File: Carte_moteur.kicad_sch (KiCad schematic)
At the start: 9 parts, among them J101 Conn_01x02, J102 Conn_01x02, J103 Conn_01x02_Socket, U403 LD1117S33TR_SOT223

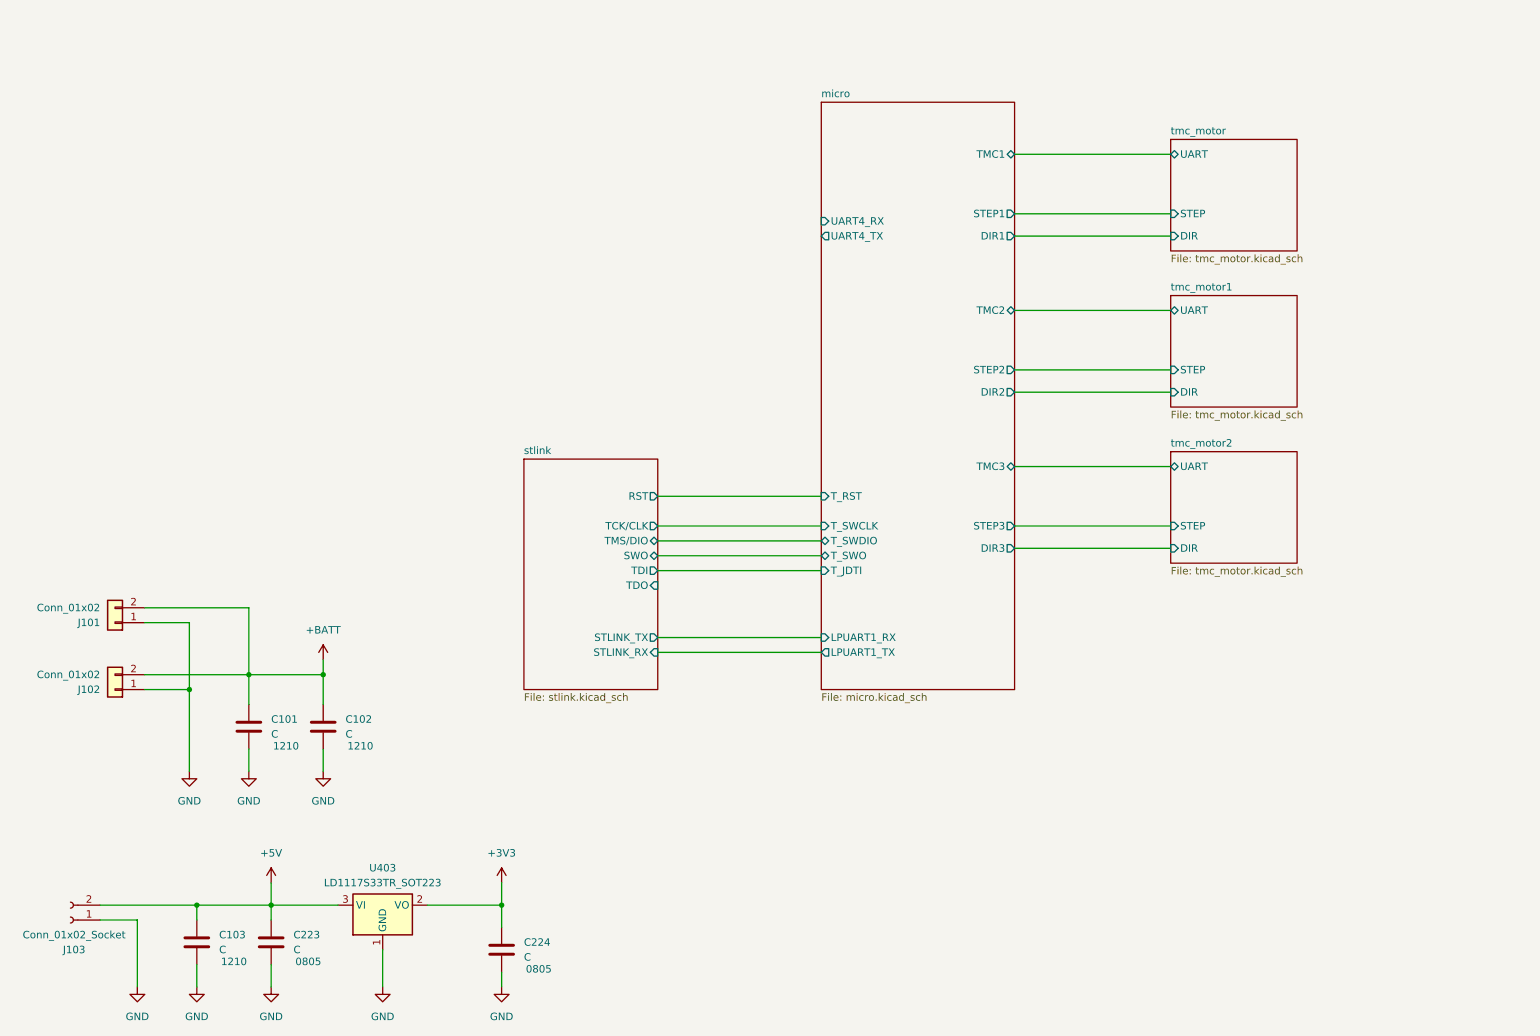
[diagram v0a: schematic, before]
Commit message: Added SPI
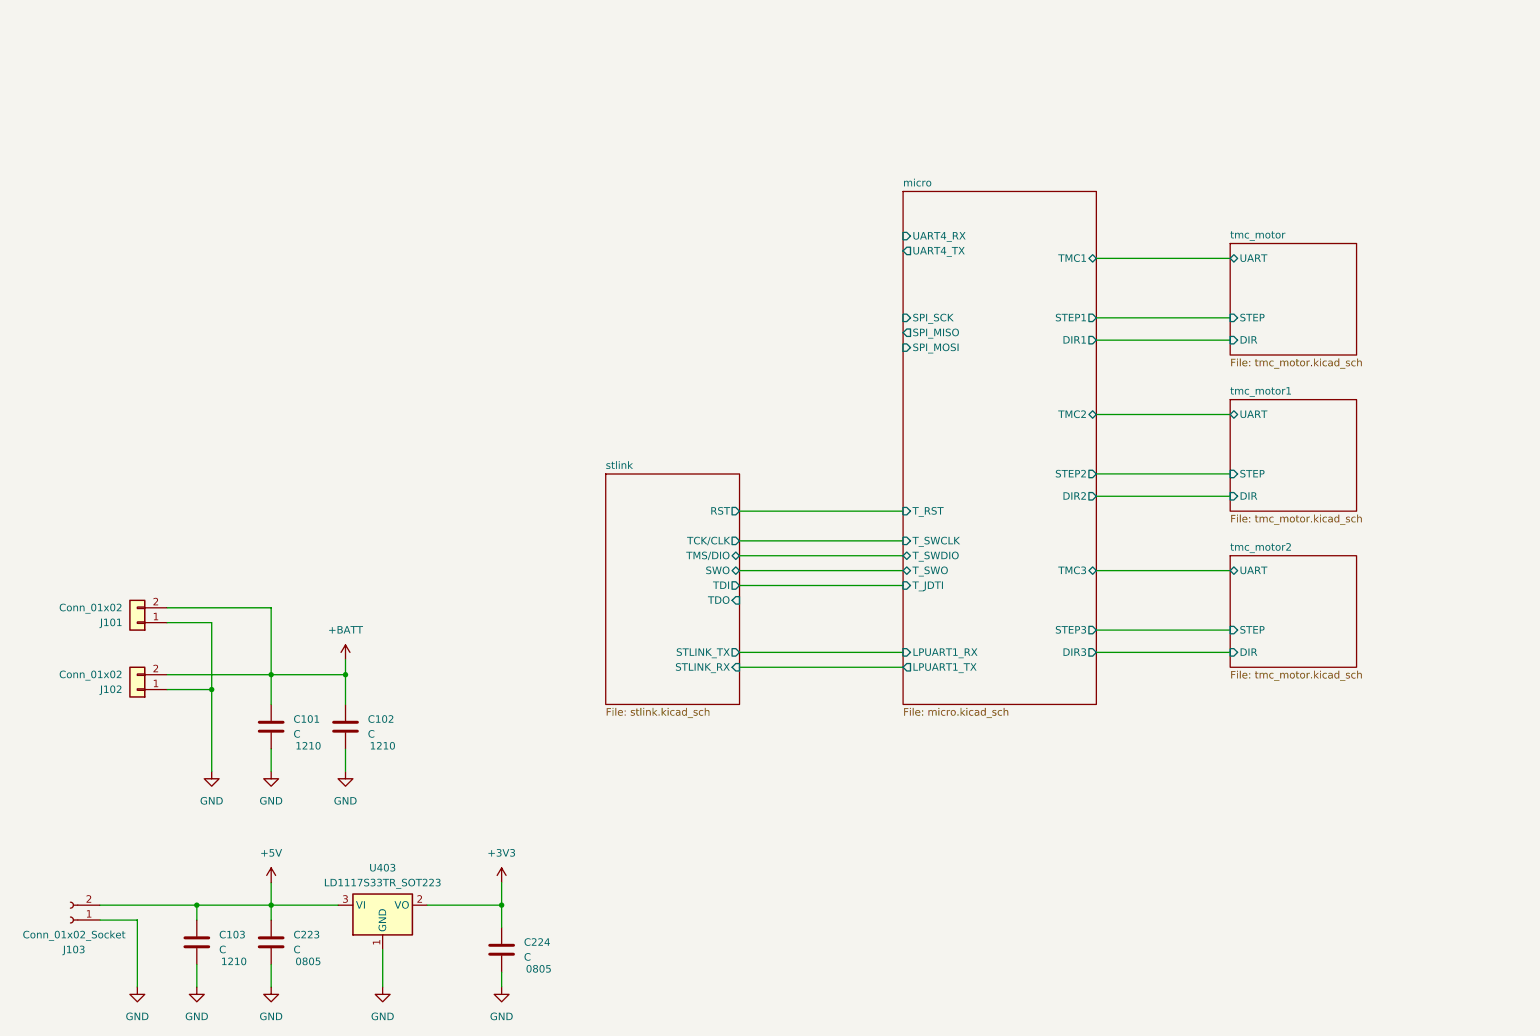
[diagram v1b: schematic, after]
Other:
- sheet micro ports: added SPI_MISO, SPI_MOSI, SPI_SCK; removed none
- moved on the sheet: C101, C102, J101, J102

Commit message: starting layout
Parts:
- J102: renamed from J101; footprint (none) -> Connector_Molex:Molex_KK-396_A-41791-0002_1x02_P3.96mm_Vertical
- J103: renamed from J102; footprint (none) -> Connector_Molex:Molex_KK-396_A-41791-0002_1x02_P3.96mm_Vertical
- renumbered C103 to C101, C101 to C102, C223 to C103, C102 to C104, C224 to C105, J103 to J101, U403 to U101
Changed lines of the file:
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@@
 		(dnp no)
 		(fields_autoplaced yes)
-		(property "Reference" "#PWR0284"
+		(property "Reference" "#PWR0107"
 			(at 71.12 133.35 0)
 			(effects
@@
 			(project "Carte_moteur"
 				(path "/5d858058-eb89-4613-a7ba-0652b9f0936c"
-					(reference "#PWR0284")
+					(reference "#PWR0107")
 					(unit 1)
 				)
@@
 		(on_board yes)
 		(dnp no)
-		(property "Reference" "C223"
+		(property "Reference" "C103"
 			(at 62.23 176.5299 0)
 			(effects
@@
 			(project "Carte_moteur"
 				(path "/5d858058-eb89-4613-a7ba-0652b9f0936c"
-					(reference "C223")
+					(reference "C103")
 					(unit 1)
 				)
@@
 		(dnp no)
 		(fields_autoplaced yes)
-		(property "Reference" "#PWR0291"
+		(property "Reference" "#PWR0110"
 			(at 97.79 171.45 0)
 			(effects
@@
 			(project "Carte_moteur"
 				(path "/5d858058-eb89-4613-a7ba-0652b9f0936c"
-					(reference "#PWR0291")
+					(reference "#PWR0110")
 					(unit 1)
 				)
@@
 		(on_board yes)
 		(dnp no)
-		(property "Reference" "C103"
+		(property "Reference" "C101"
 			(at 49.53 176.5299 0)
 			(effects
@@
 			(project "Carte_moteur"
 				(path "/5d858058-eb89-4613-a7ba-0652b9f0936c"
-					(reference "C103")
+					(reference "C101")
 					(unit 1)
 				)
@@
 		(dnp no)
 		(fields_autoplaced yes)
-		(property "Reference" "#PWR0293"
+		(property "Reference" "#PWR0101"
 			(at 35.56 191.77 0)
 			(effects
@@
 			(project "Carte_moteur"
 				(path "/5d858058-eb89-4613-a7ba-0652b9f0936c"
-					(reference "#PWR0293")
+					(reference "#PWR0101")
 					(unit 1)
 				)
@@
 		(on_board yes)
 		(dnp no)
-		(property "Reference" "C101"
+		(property "Reference" "C102"
 			(at 62.23 139.6999 0)
 			(effects
@@
 			(project "Carte_moteur"
 				(path "/5d858058-eb89-4613-a7ba-0652b9f0936c"
-					(reference "C101")
+					(reference "C102")
 					(unit 1)
 				)
@@
 		(on_board yes)
 		(dnp no)
-		(property "Reference" "J101"
+		(property "Reference" "J102"
 			(at 33.02 123.1901 0)
 			(effects
@@
 			)
 		)
-		(property "Footprint" ""
+		(property "Footprint" "Connector_Molex:Molex_KK-396_A-41791-0002_1x02_P3.96mm_Vertical"
 			(at 35.56 123.19 0)
 			(effects
@@
 			(project ""
 				(path "/5d858058-eb89-4613-a7ba-0652b9f0936c"
-					(reference "J101")
+					(reference "J102")
 					(unit 1)
 				)
@@
 		(dnp no)
 		(fields_autoplaced yes)
-		(property "Reference" "#PWR0289"
+		(property "Reference" "#PWR0109"
 			(at 77.47 191.77 0)
 			(effects
@@
 			(project "Carte_moteur"
 				(path "/5d858058-eb89-4613-a7ba-0652b9f0936c"
-					(reference "#PWR0289")
+					(reference "#PWR0109")
 					(unit 1)
 				)
@@
 		(on_board yes)
 		(dnp no)
-		(property "Reference" "#PWR0286"
+		(property "Reference" "#PWR0108"
 			(at 71.12 154.94 0)
 			(effects
@@
 			(project "Carte_moteur"
 				(path "/5d858058-eb89-4613-a7ba-0652b9f0936c"
-					(reference "#PWR0286")
+					(reference "#PWR0108")
 					(unit 1)
 				)
@@
 		(dnp no)
 		(fields_autoplaced yes)
-		(property "Reference" "#PWR0416"
+		(property "Reference" "#PWR0105"
 			(at 58.42 171.45 0)
 			(effects
@@
 			(project "Carte_moteur"
 				(path "/5d858058-eb89-4613-a7ba-0652b9f0936c"
-					(reference "#PWR0416")
+					(reference "#PWR0105")
 					(unit 1)
 				)
@@
 		(on_board yes)
 		(dnp no)
-		(property "Reference" "C102"
+		(property "Reference" "C104"
 			(at 74.93 139.6999 0)
 			(effects
@@
 			(project "Carte_moteur"
 				(path "/5d858058-eb89-4613-a7ba-0652b9f0936c"
-					(reference "C102")
+					(reference "C104")
 					(unit 1)
 				)
@@
 		(on_board yes)
 		(dnp no)
-		(property "Reference" "#PWR0287"
+		(property "Reference" "#PWR0103"
 			(at 48.26 154.94 0)
 			(effects
@@
 			(project "Carte_moteur"
 				(path "/5d858058-eb89-4613-a7ba-0652b9f0936c"
-					(reference "#PWR0287")
+					(reference "#PWR0103")
 					(unit 1)
 				)
@@
 		(on_board yes)
 		(dnp no)
-		(property "Reference" "#PWR0285"
+		(property "Reference" "#PWR0104"
 			(at 58.42 154.94 0)
 			(effects
@@
 			(project "Carte_moteur"
 				(path "/5d858058-eb89-4613-a7ba-0652b9f0936c"
-					(reference "#PWR0285")
+					(reference "#PWR0104")
 					(unit 1)
 				)
@@
 		(dnp no)
 		(fields_autoplaced yes)
-		(property "Reference" "U403"
+		(property "Reference" "U101"
 			(at 77.47 165.1 0)
 			(effects
@@
 			(project "Carte_moteur"
 				(path "/5d858058-eb89-4613-a7ba-0652b9f0936c"
-					(reference "U403")
+					(reference "U101")
 					(unit 1)
 				)
@@
 		(on_board yes)
 		(dnp no)
-		(property "Reference" "J102"
+		(property "Reference" "J103"
 			(at 33.02 134.6201 0)
 			(effects
@@
 			)
 		)
-		(property "Footprint" ""
+		(property "Footprint" "Connector_Molex:Molex_KK-396_A-41791-0002_1x02_P3.96mm_Vertical"
 			(at 35.56 134.62 0)
 			(effects
@@
 			(project "Carte_moteur"
 				(path "/5d858058-eb89-4613-a7ba-0652b9f0936c"
-					(reference "J102")
+					(reference "J103")
 					(unit 1)
 				)
@@
 		(dnp no)
 		(fields_autoplaced yes)
-		(property "Reference" "#PWR0288"
+		(property "Reference" "#PWR0106"
 			(at 58.42 191.77 0)
 			(effects
@@
 			(project "Carte_moteur"
 				(path "/5d858058-eb89-4613-a7ba-0652b9f0936c"
-					(reference "#PWR0288")
+					(reference "#PWR0106")
 					(unit 1)
 				)
@@
 		(on_board yes)
 		(dnp no)
-		(property "Reference" "J103"
+		(property "Reference" "J101"
 			(at 24.765 179.07 0)
 			(effects
@@
 			(project ""
 				(path "/5d858058-eb89-4613-a7ba-0652b9f0936c"
-					(reference "J103")
+					(reference "J101")
 					(unit 1)
 				)
@@
 		(on_board yes)
 		(dnp no)
-		(property "Reference" "C224"
+		(property "Reference" "C105"
 			(at 101.6 177.7999 0)
 			(effects
@@
 			(project "Carte_moteur"
 				(path "/5d858058-eb89-4613-a7ba-0652b9f0936c"
-					(reference "C224")
+					(reference "C105")
 					(unit 1)
 				)
@@
 		(dnp no)
 		(fields_autoplaced yes)
-		(property "Reference" "#PWR0292"
+		(property "Reference" "#PWR0102"
 			(at 45.72 191.77 0)
 			(effects
@@
 			(project "Carte_moteur"
 				(path "/5d858058-eb89-4613-a7ba-0652b9f0936c"
-					(reference "#PWR0292")
+					(reference "#PWR0102")
 					(unit 1)
 				)
@@
 		(dnp no)
 		(fields_autoplaced yes)
-		(property "Reference" "#PWR0290"
+		(property "Reference" "#PWR0111"
 			(at 97.79 191.77 0)
 			(effects
@@
 			(project "Carte_moteur"
 				(path "/5d858058-eb89-4613-a7ba-0652b9f0936c"
-					(reference "#PWR0290")
-					(unit 1)
-				)
+					(reference "#PWR0111")
+					(unit 1)
+				)

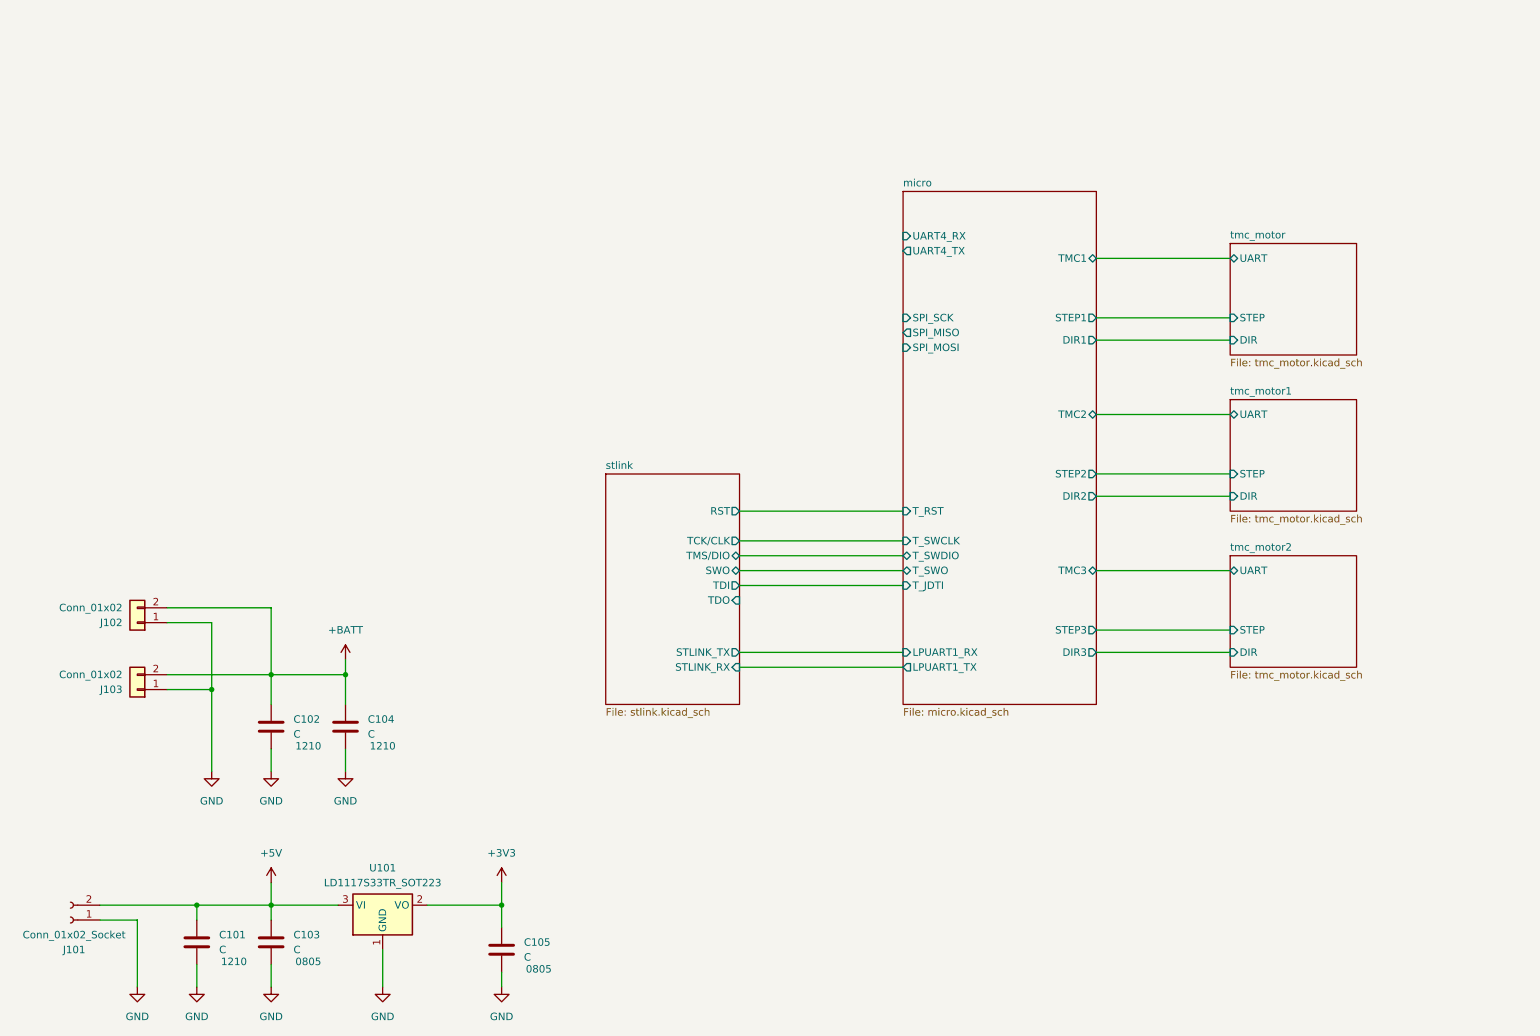
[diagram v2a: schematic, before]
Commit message: quadrature encoder added
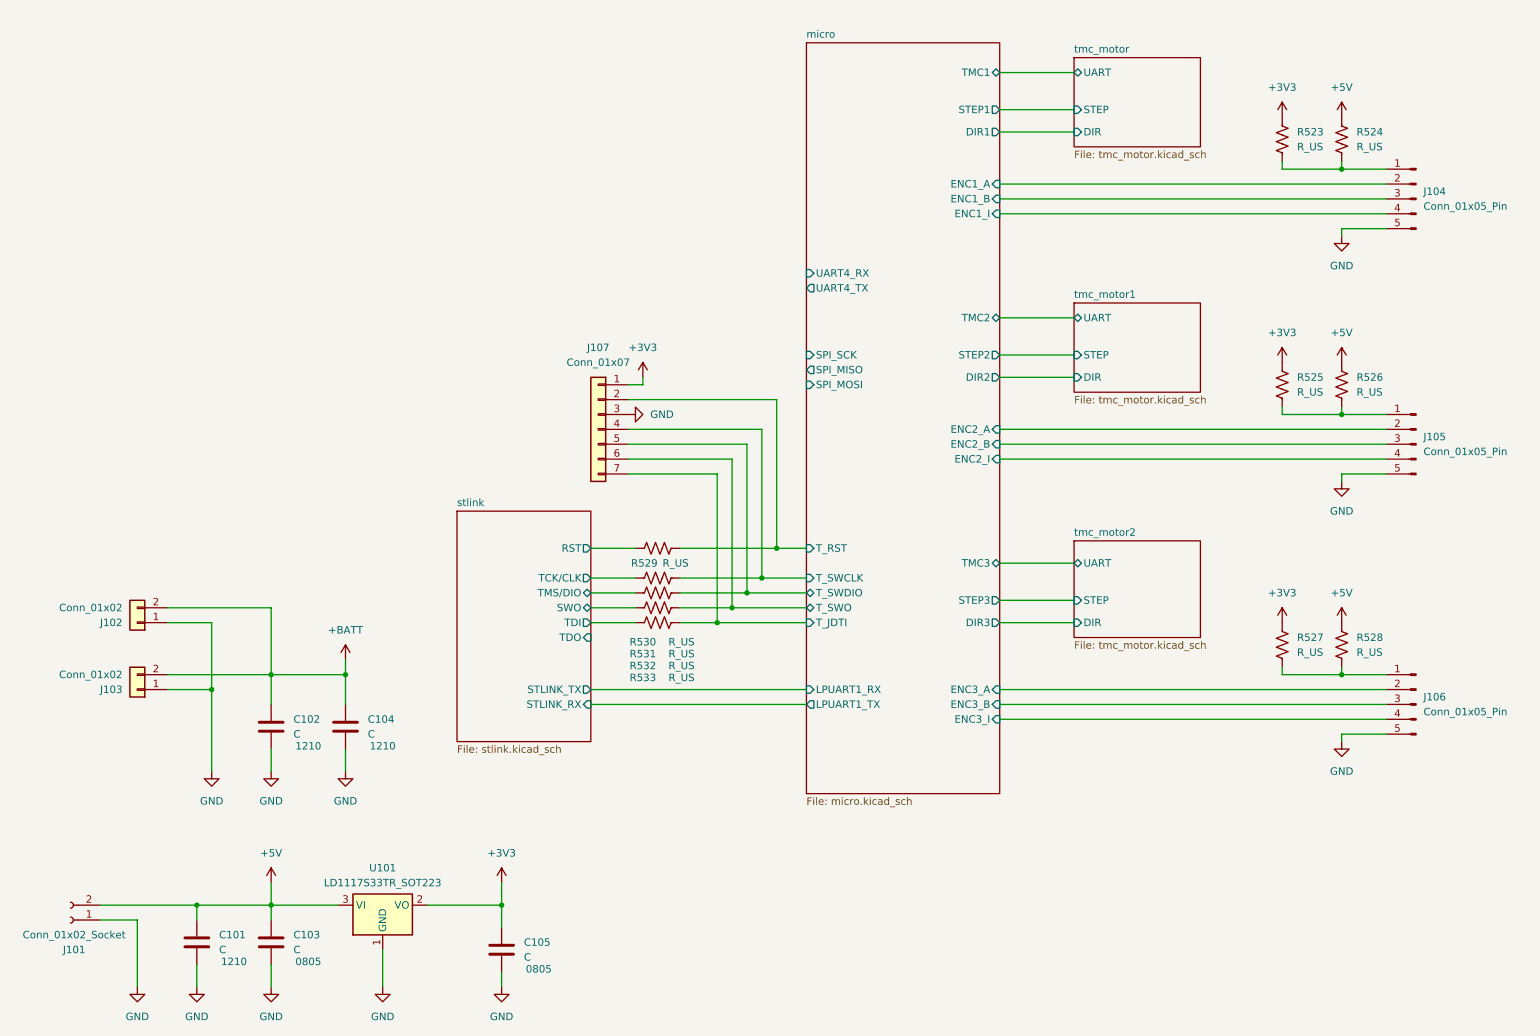
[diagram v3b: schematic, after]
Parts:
- added J104, J105, J106: Conn_01x05_Pin, Connector_Molex:Molex_KK-254_AE-6410-05A_1x05_P2.54mm_Vertical, symbol Connector:Conn_01x05_Pin
- added J107: Conn_01x07, Connector_Molex:Molex_KK-254_AE-6410-07A_1x07_P2.54mm_Vertical, symbol Connector_Generic:Conn_01x07
- added R523, R524, R525, R526, R527, R528, R529, R530, R531, R532, R533: R_US, Resistor_SMD:R_0603_1608Metric_Pad0.98x0.95mm_HandSolder, symbol Device:R_US
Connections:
- net +3V3: now also J107.1 (Pin_1), R523.2, R525.2, R527.2
- net +5V: now also R524.2, R526.2, R528.2
- net GND: now also J104.5 (Pin_5), J105.5 (Pin_5), J106.5 (Pin_5), J107.3 (Pin_3)
- net micro/T_JDTI: now also J107.7 (Pin_7), R533.1
- net micro/T_RST: now also J107.2 (Pin_2), R529.1
- net micro/T_SWCLK: now also J107.4 (Pin_4), R530.1
- net micro/T_SWDIO: now also J107.5 (Pin_5), R531.1
- net micro/T_SWO: now also J107.6 (Pin_6), R532.1
- new net: J106.1 (Pin_1), R527.1, R528.1
- new net: J104.1 (Pin_1), R523.1, R524.1
- new net: J105.1 (Pin_1), R525.1, R526.1
- new net micro/ENC1_A: J104.2 (Pin_2)
- new net micro/ENC1_B: J104.3 (Pin_3)
- new net micro/ENC1_I: J104.4 (Pin_4)
- new net micro/ENC2_A: J105.2 (Pin_2)
- new net micro/ENC2_B: J105.3 (Pin_3)
- new net micro/ENC2_I: J105.4 (Pin_4)
- new net micro/ENC3_A: J106.2 (Pin_2)
- new net micro/ENC3_B: J106.3 (Pin_3)
- new net micro/ENC3_I: J106.4 (Pin_4)
- new net stlink/RST: R529.2
- new net stlink/SWO: R532.2
- new net stlink/TCK/CLK: R530.2
- new net stlink/TDI: R533.2
- new net stlink/TMS/DIO: R531.2
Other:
- sheet micro ports: added ENC1_A, ENC1_B, ENC1_I, ENC2_A, ENC2_B, ENC2_I, ENC3_A, ENC3_B, ENC3_I; removed none
